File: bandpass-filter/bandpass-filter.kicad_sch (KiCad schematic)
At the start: 3 parts

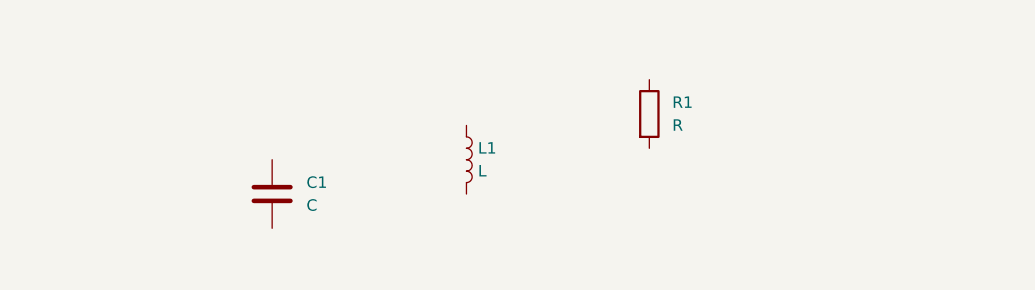
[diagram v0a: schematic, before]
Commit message: Schematic and Spice simulation complete, missing layout and EMerge simulation.
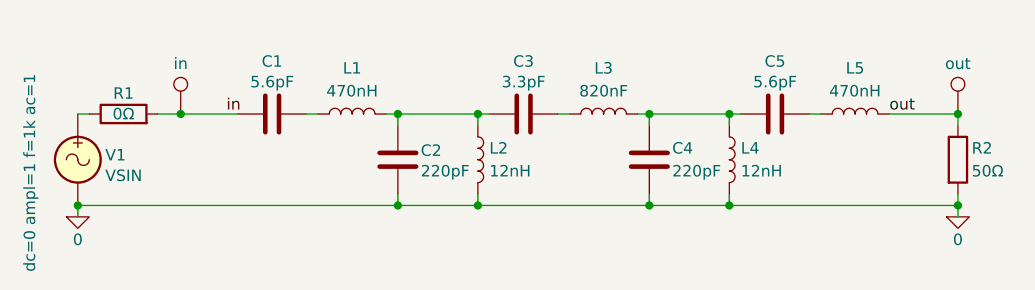
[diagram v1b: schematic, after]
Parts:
- added C2, C4: 220pF, FEM-Solver:C_0603_1608Metric_femSolver, symbol Device:C
- added C3: 3.3pF, FEM-Solver:C_0603_1608Metric_femSolver, symbol Device:C
- added C5: 5.6pF, FEM-Solver:C_0603_1608Metric_femSolver, symbol Device:C
- added L2, L4: 12nH, FEM-Solver:L_0603_1608Metric_femSolver, symbol Device:L
- added L3: 820nF, FEM-Solver:L_0603_1608Metric_femSolver, symbol Device:L
- added L5: 470nH, FEM-Solver:L_0603_1608Metric_femSolver, symbol Device:L
- added R1: 0Ω, symbol Device:R
- added TP1: in, TestPoint:TestPoint_Pad_1.0x1.0mm, symbol Connector:TestPoint
- added TP2: out, TestPoint:TestPoint_Pad_1.0x1.0mm, symbol Connector:TestPoint
- added V1: VSIN, symbol Simulation_SPICE:VSIN
- C1: value C -> 5.6pF; footprint (none) -> FEM-Solver:C_0603_1608Metric_femSolver
- L1: value L -> 470nH; footprint (none) -> FEM-Solver:L_0603_1608Metric_femSolver
- R2: renamed from R1; value R -> 50Ω
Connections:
- net at L1.1: now also C1.2
- net at L1.2: now also C2.1, C3.1, L2.1
- net out: now reaches R2.1
- net out: now also L5.2, TP2.1
- net 0: now reaches R2.2
- net 0: now also C2.2, C4.2, L2.2, L4.2, V1.2
- net in: now reaches C1.1
- net in: now also R1.2, TP1.1
- new net: C3.2, L3.1
- new net: C4.1, C5.1, L3.2, L4.1
- new net: C5.2, L5.1
- new net: R1.1, V1.1
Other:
- moved on the sheet: C1, L1, R2

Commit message: Changing PCB layout.
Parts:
- C1, C5: value 5.6pF -> 5.6p
- C2, C4: value 220pF -> 220p
- C3: value 3.3pF -> 3.3p
- L1, L5: value 470nH -> 470n
- L2, L4: value 12nH -> 12n
- L3: value 820nF -> 820n
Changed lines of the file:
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@@
 			)
 		)
-		(property "Value" "3.3pF"
+		(property "Value" "3.3p"
 			(at 97.79 44.704 90)
 			(effects
@@
 			)
 		)
-		(property "Value" "220pF"
+		(property "Value" "220p"
 			(at 86.36 54.61 0)
 			(effects
@@
 			)
 		)
-		(property "Value" "5.6pF"
+		(property "Value" "5.6p"
 			(at 125.73 44.704 90)
 			(effects
@@
 			)
 		)
-		(property "Value" "820nF"
+		(property "Value" "820n"
 			(at 106.68 45.72 90)
 			(effects
@@
 			)
 		)
-		(property "Value" "470nH"
+		(property "Value" "470n"
 			(at 78.74 45.72 90)
 			(effects
@@
 			)
 		)
-		(property "Value" "12nH"
+		(property "Value" "12n"
 			(at 121.92 54.6099 0)
 			(effects
@@
 			)
 		)
-		(property "Value" "12nH"
+		(property "Value" "12n"
 			(at 93.98 54.6099 0)
 			(effects
@@
 			)
 		)
-		(property "Value" "220pF"
+		(property "Value" "220p"
 			(at 114.3 54.61 0)
 			(effects
@@
 			)
 		)
-		(property "Value" "5.6pF"
+		(property "Value" "5.6p"
 			(at 69.85 44.704 90)
 			(effects
@@
 			)
 		)
-		(property "Value" "470nH"
+		(property "Value" "470n"
 			(at 134.62 45.72 90)
 			(effects
